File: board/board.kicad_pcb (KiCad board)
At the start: 2 copper layers, 21 x 13 mm, 1 part

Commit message: initial
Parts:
- removed LOGO1: Logo_Open_Hardware_Small, Symbol:OSHW-Symbol_6.7x6mm_SilkScreen
- added C1: 100n, Capacitor_SMD:C_0603_1608Metric, B.Cu at (85.0, 77.6)
- added C10: 22uF, Capacitor_SMD:C_1206_3216Metric, F.Cu at (84.7, 77.5)
- added C2: 1uF, Capacitor_SMD:C_0603_1608Metric, B.Cu at (93.2, 77.7)
- added C3: 2.2uF, Capacitor_SMD:C_1210_3225Metric, F.Cu at (84.7, 80.3)
- added C4: 10uF, Capacitor_SMD:C_1210_3225Metric, F.Cu at (84.7, 83.5)
- added C6: 100uF, Capacitor_SMD:C_1206_3216Metric, F.Cu at (84.7, 75.2)
- added D1: SL310A-TP, Diode_SMD:D_SMA, F.Cu at (90.6, 85.1)
- added J1: 013_PoE_rectified, on_edge:on_edge_2x05_device, F.Cu at (77.0, 80.6)
- added J2: 003_power, on_edge:on_edge_2x05_host, F.Cu at (114.0, 80.5)
- added L1: 22uH, Inductor_SMD:L_2512_6332Metric, F.Cu at (90.9, 79.5)
- added R1: 59k, Resistor_SMD:R_0603_1608Metric, B.Cu at (88.6, 75.9)
- added R2: 100k, Resistor_SMD:R_0603_1608Metric, B.Cu at (90.1, 75.9)
- added R3: 41.2R, Resistor_SMD:R_0603_1608Metric, B.Cu at (85.0, 80.6)
- added R4: 24.9k, Resistor_SMD:R_0603_1608Metric, B.Cu at (86.6, 75.9)
- added R5: 43.2k, Resistor_SMD:R_0603_1608Metric, B.Cu at (91.7, 75.9)
- added U1: MP8007, Package_DFN_QFN:QFN-28-1EP_4x5mm_P0.5mm_EP2.65x3.65mm_ThermalVias, B.Cu at (88.9, 80.1)
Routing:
- net /Controller/5V: track 0.00 -> 65.4 mm, vias 0 -> 3
- net /Controller/GNDPWR: track 0.00 -> 48.8 mm, vias 0 -> 2
- net GND: track 0.00 -> 37.6 mm, vias 0 -> 3
- net Net-(J1-Pad9): track 0.00 -> 35.1 mm
- net /Controller/PoE-: track 0.00 -> 21.1 mm, vias 0 -> 1
- net /Controller/SW: track 0.00 -> 17.2 mm, vias 0 -> 6
- net /Controller/FB2: track 0.00 -> 3.66 mm
- net /Controller/VCC: track 0.00 -> 2.19 mm
- net /Controller/ILIM: track 0.00 -> 1.92 mm
- net /Controller/DET: track 0.00 -> 1.91 mm
- net /Controller/CLASS: track 0.00 -> 1.50 mm
- added copper zone on B.Cu, net /Controller/GNDPWR
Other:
- board size 21 x 13 mm -> 37 x 13 mm
- rule pad_to_mask_clearance: 0 -> 0.04
- board text added: "osf.003"
- board text added: "osf.013"
- board text added: "osf.b051.v1.0"

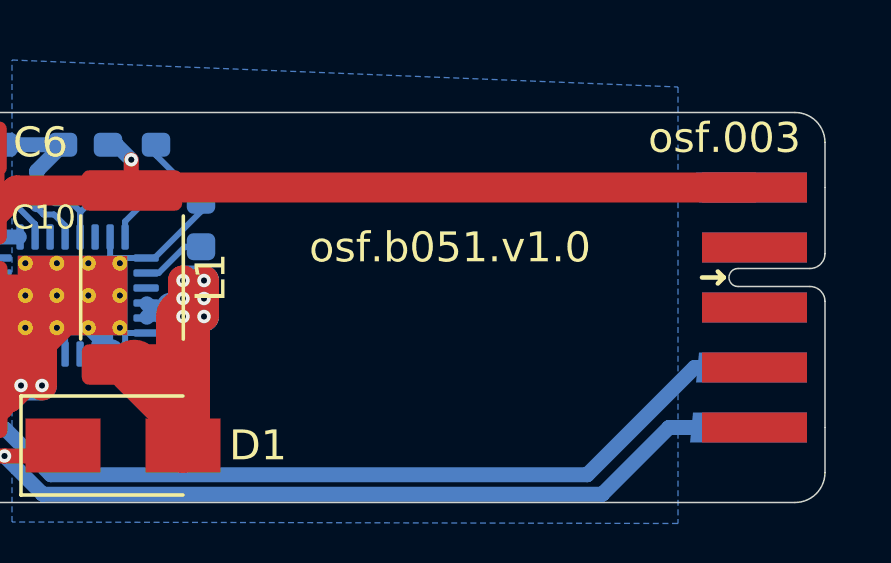
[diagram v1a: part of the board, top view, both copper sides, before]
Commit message: fixed board number on silkscreen
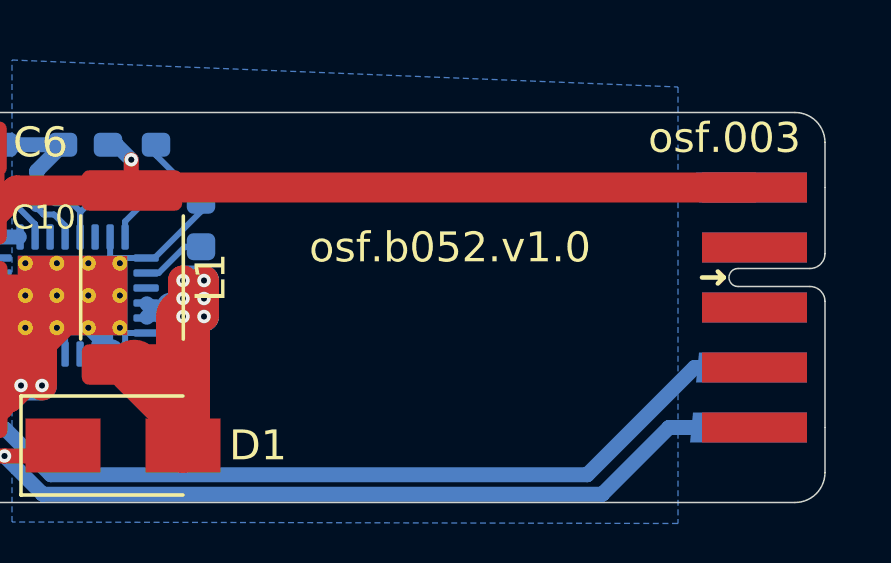
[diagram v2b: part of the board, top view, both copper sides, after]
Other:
- board text added: "osf.b052.v1.0"
- board text removed: "osf.b051.v1.0"
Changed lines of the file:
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@@
     (descr "Inductor SMD 2512 (6332 Metric), square (rectangular) end terminal, IPC_7351 nominal, (Body size source: http://www.tortai-tech.com/upload/download/2011102023233369053.pdf), generated with kicad-footprint-generator")
     (tags "inductor")
+    (property "Digi-Key_PN" "587-6228-1-ND")
+    (property "MPN" "EST0645T220MDGA")
     (property "Sheetfile" "Controller.kicad_sch")
     (property "Sheetname" "Controller")
@@
     (effects (font (size 1 1) (thickness 0.15)))
   )
-  (gr_text "osf.b051.v1.0" (at 101.5 78.5) (layer "F.SilkS")
+  (gr_text "osf.b052.v1.0" (at 101.5 78.5) (layer "F.SilkS")
     (effects (font (size 1 1) (thickness 0.15)))
   )
